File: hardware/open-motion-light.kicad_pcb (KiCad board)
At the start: 2 copper layers, 77 x 73 mm, 93 parts, among them J1 TYPE-C-31-M-12, Q1 2N7002, SW1 SW_Push, SW2 SW_Push, SW3 SSSS213800, U1 CN3058E, U2 VCNL4020-GS08, U3 MT9284BS6, U4 PIR223D-S0, U6 CH340X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

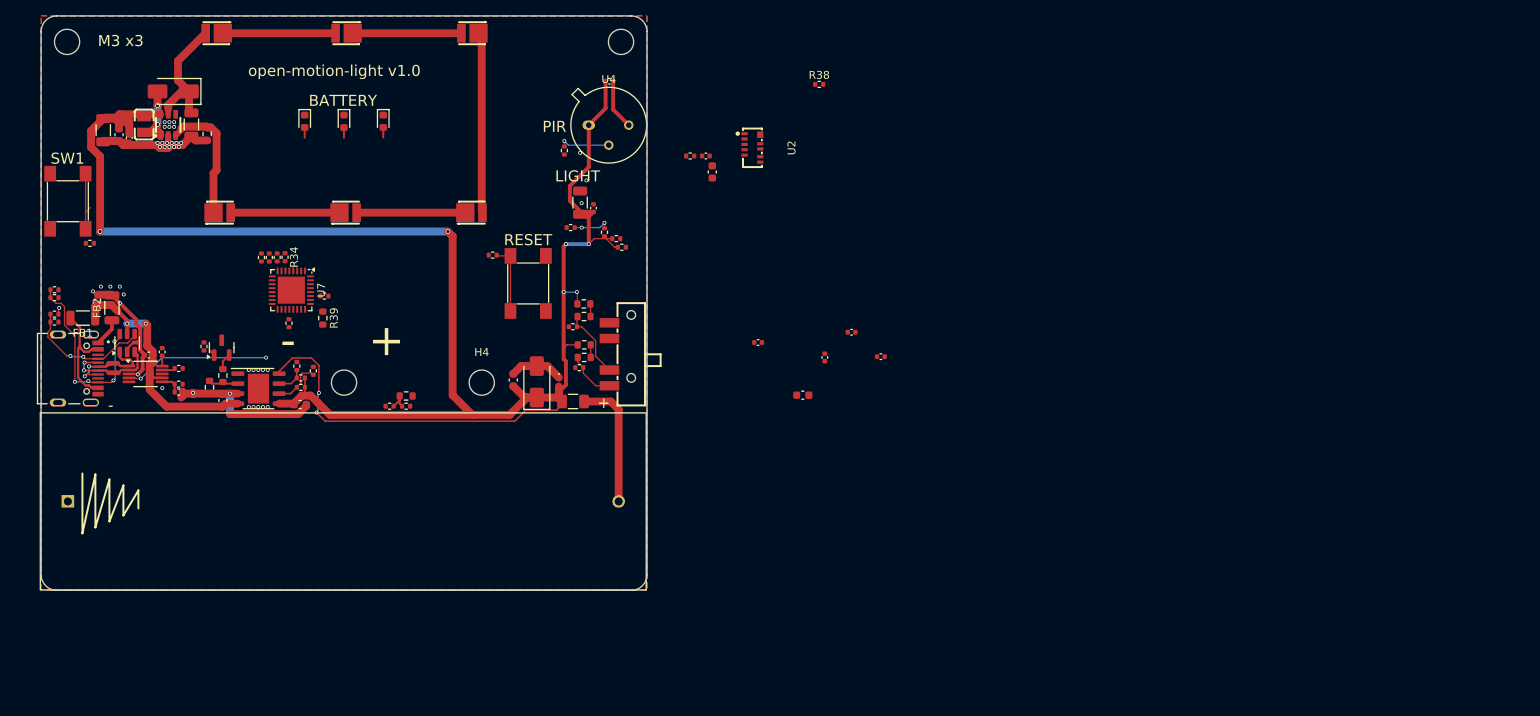
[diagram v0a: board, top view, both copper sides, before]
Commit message: Update PCB for circle layout
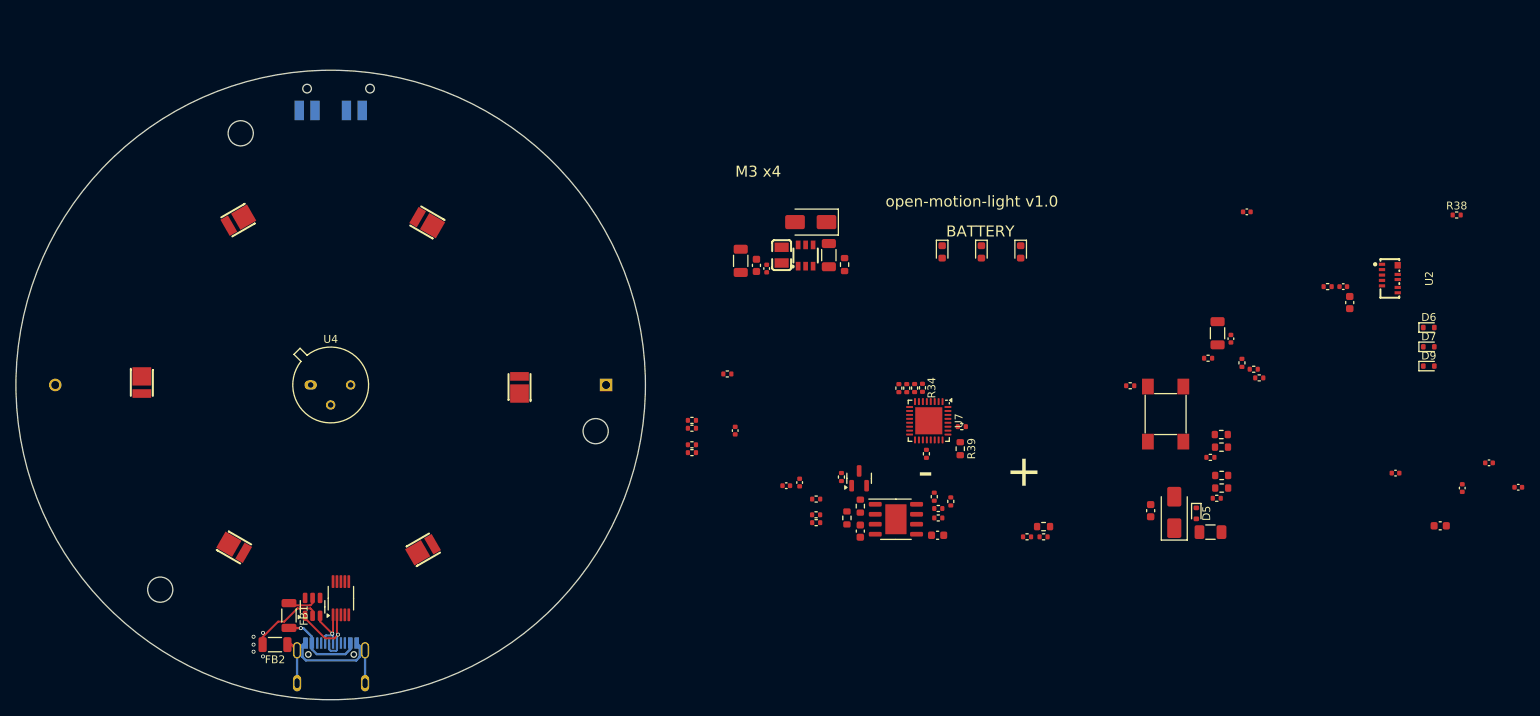
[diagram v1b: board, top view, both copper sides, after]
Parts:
- removed H4: MountingHole, MountingHole:MountingHole_3.2mm_M3_ISO7380
- removed R17: 1k, Resistor_SMD:R_0402_1005Metric
- removed SW2: SW_Push, Homebrew:SW_TACTILE_5.1MM_TS-1187A-C-D-B
- added D6: ESD5Z5.0, Diode_SMD:D_SOD-523, F.Cu at (227.4, 102.6)
- added D7: ESD5Z5.0, Diode_SMD:D_SOD-523, F.Cu at (227.4, 105.0)
- added D9: ESD5Z5.0, Diode_SMD:D_SOD-523, F.Cu at (227.4, 107.5)
- BT1, J1, SW3: moved to B.Cu
- D5: value D_TVS -> ESD5Z5.0; footprint Diode_SMD:D_0402_1005Metric -> Diode_SMD:D_SOD-523
- F1: value Polyfuse 1A -> BSMD1206-100-6V
- R2: value 1k2 -> 1k5
- R26, R30, R31: value 1k -> 10k
- moved C1 82.7 mm to (155.1, 128.5)
- moved C11 82.7 mm to (151.1, 93.4)
- moved C12 82.7 mm to (216.5, 97.4)
- moved C7 82.7 mm to (231.6, 123.0)
- moved F1 82.7 mm to (199.6, 128.6)
- moved L2 82.7 mm to (145.1, 93.4)
- moved R18 82.7 mm to (203.6, 107.1)
- moved R2 82.7 mm to (155.1, 125.3)
- moved R20 82.7 mm to (205.1, 107.9)
- moved R25 82.7 mm to (153.1, 94.6)
- moved R36 82.7 mm to (201.0, 116.2)
- moved R38 82.7 mm to (230.9, 88.3)
- moved R8 82.7 mm to (166.6, 124.7)
- moved C16 82.7 mm to (147.4, 122.3)
- moved C18 82.7 mm to (202.2, 104.0)
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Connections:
- D1 pad 1: /USB_DP -> /USB_DN
- D1 pad 3: /USB_DN -> /USB_DP
- D5 pad 1: GND -> Net-(D5-K)
- D5 pad 2: VCC -> GND
- J1 pad S1: unconnected-(J1-SHIELD-PadS1) -> Net-(FB2-Pad1)
- J1 pad S2: unconnected-(J1-SHIELD-PadS1)_2 -> Net-(FB2-Pad1)
- J1 pad S3: unconnected-(J1-SHIELD-PadS1)_1 -> Net-(FB2-Pad1)
- J1 pad S4: unconnected-(J1-SHIELD-PadS1)_0 -> Net-(FB2-Pad1)
- R26 pad 1: Net-(R26-Pad1) -> Net-(D9-K)
- R26 pad 2: /BUTTON -> /PIR
- R28 pad 2: Net-(R28-Pad2) -> Net-(D5-K)
- R31 pad 1: Net-(R28-Pad2) -> Net-(D5-K)
- SW3 pad 2: Net-(R28-Pad2) -> Net-(D5-K)
- U4 pad 2: Net-(U4-RELOUT) -> Net-(D9-K)
- U7 pad 23: /SWDIO -> unconnected-(U7-PA13-Pad23)
- U7 pad 24: /SWCLK -> unconnected-(U7-PA14-Pad24)
- U7 pad 28: /BUTTON -> unconnected-(U7-PB5-Pad28)
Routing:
- net VCC: track 254.3 -> 0.00 mm, vias 8 -> 0
- net GND: track 73.9 -> 9.59 mm, vias 40 -> 5
- net +5V: track 36.6 -> 4.24 mm, vias 2 -> 0
- net /CC2_RAW: track 24.4 -> 0.00 mm, vias 4 -> 0
- net Net-(LED3-Pad1): track 23.0 -> 0.00 mm
- net Net-(FB2-Pad1): track 3.63 -> 23.7 mm
- net Net-(U3-FB): track 19.4 -> 0.00 mm
- net /~{RTS}: track 18.6 -> 0.00 mm, vias 2 -> 0
- net /CC1_RAW: track 17.3 -> 0.00 mm, vias 2 -> 0
- net Net-(D8-K): track 16.8 -> 0.00 mm
- net Net-(BT1-Pad2): track 16.5 -> 0.00 mm
- net Net-(LED1-Pad1): track 14.3 -> 0.00 mm
- net Net-(LED5-Pad1): track 13.8 -> 0.00 mm
- net Net-(LED4-Pad1): track 13.8 -> 0.00 mm
- net Net-(LED2-Pad1): track 13.8 -> 0.00 mm
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- added copper zone on In1.Cu, net GND
- added copper zone on In2.Cu, net GND
- removed copper zone on B.Cu, net GND
- removed copper zone on F.Cu, net GND
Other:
- board size 77 x 73 mm -> 80 x 80 mm
- copper layers 2 -> 4
- board text added: "M3 x4"
- board text removed: "LIGHT"
- board text removed: "M3 x3"
- board text removed: "PIR"
- board text removed: "RESET"
- board text removed: "SW1"

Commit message: Place and route LEDs, driver, and USB power
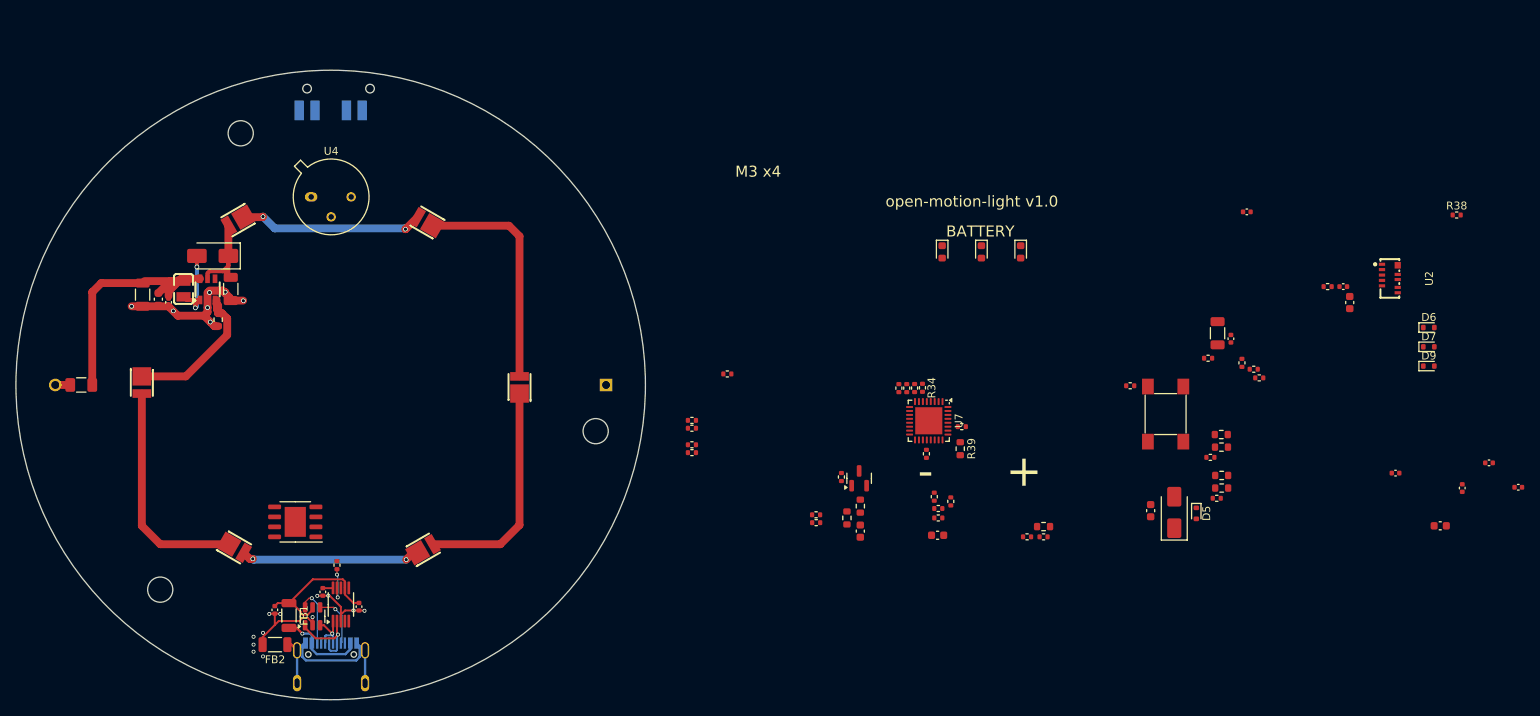
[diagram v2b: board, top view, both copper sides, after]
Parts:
- moved F1 144.7 mm to (56.1, 109.9), turned to 180 degrees
- moved R25 79.9 mm to (73.5, 101.6)
- moved U1 76.3 mm to (83.3, 127.3), turned to 180 degrees
- moved C11 76.1 mm to (75.1, 97.7)
- moved L2 76.1 mm to (69.1, 97.7)
- moved C9 76.1 mm to (67.2, 99.4)
- moved D8 76.1 mm to (72.8, 93.5)
- moved C10 76.1 mm to (65.9, 99.0)
- moved C13 76.1 mm to (63.9, 98.4)
- moved U3 76.1 mm to (72.2, 97.8)
- moved C2 62.8 mm to (80.7, 138.5), turned to -90 degrees
- moved C16 62.2 mm to (86.8, 136.2), turned to -90 degrees
- moved R22 61.5 mm to (88.6, 132.8), turned to 90 degrees
- moved C15 56.4 mm to (91.4, 138.1), turned to -90 degrees
- moved U4 23.9 mm to (85.3, 86.0)
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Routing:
- net GND: track 9.59 -> 59.2 mm, vias 5 -> 19
- net VCC: track 0.00 -> 38.5 mm
- net Net-(LED2-Pad1): track 0.00 -> 29.4 mm
- net Net-(LED5-Pad1): track 0.00 -> 28.8 mm
- net Net-(LED3-Pad1): track 0.00 -> 28.8 mm
- net Net-(LED1-Pad1): track 0.00 -> 23.4 mm, vias 0 -> 2
- net Net-(LED4-Pad1): track 0.00 -> 22.8 mm, vias 0 -> 2
- net Net-(U3-FB): track 0.00 -> 20.2 mm
- net +5V: track 4.24 -> 19.2 mm
- net Net-(D8-K): track 0.00 -> 13.0 mm
- net Net-(D8-A): track 0.00 -> 11.4 mm, vias 0 -> 2
- net /CC2_RAW: track 0.00 -> 7.71 mm, vias 0 -> 1
- net /CC1_RAW: track 0.00 -> 6.75 mm, vias 0 -> 1
- net Net-(U6-RXD): track 0.00 -> 4.89 mm, vias 0 -> 2
- net Net-(BT1-Pad2): track 0.00 -> 1.90 mm
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
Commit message: Hardware revision v1.1
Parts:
- R11, R12: value 1k -> 10k
- moved D6 169.4 mm to (58.2, 111.8)
- moved C6 164.1 mm to (74.7, 118.8), turned to 0 degrees
- moved C5 155.9 mm to (79.3, 111.5)
- moved C7 155.5 mm to (76.6, 111.1)
- moved R38 155.4 mm to (76.8, 108.5)
- moved C4 150.6 mm to (79.3, 109.7)
- moved D7 145.1 mm to (84.8, 78.0), turned to -90 degrees
- moved D9 142.2 mm to (85.9, 93.0), turned to 180 degrees
- moved U2 139.6 mm to (87.8, 133.5), turned to 180 degrees
- moved C20 138.2 mm to (83.4, 133.4)
- moved C12 136.6 mm to (84.6, 133.0), turned to 90 degrees
- moved D13 135.9 mm to (59.6, 114.4), turned to 0 degrees
- moved C8 134.9 mm to (58.3, 107.9), turned to 0 degrees
- moved R37 134.1 mm to (84.7, 131.0), turned to 90 degrees
- moved C17 132.5 mm to (91.9, 139.6)
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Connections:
- C6 pad 1: VCC -> GND
- C6 pad 2: GND -> VCC
- R37 pad 1: VCC -> Net-(U2-VDD)
- R37 pad 2: Net-(U2-VDD) -> VCC
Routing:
- net VCC: track 38.5 -> 275.4 mm, vias 0 -> 19
- net GND: track 59.2 -> 145.2 mm, vias 19 -> 187
- net Net-(D4-A): track 0.00 -> 72.0 mm, vias 0 -> 2
- net Net-(D3-A): track 0.00 -> 68.8 mm, vias 0 -> 2
- net /POWER_ON: track 0.00 -> 68.2 mm, vias 0 -> 4
- net Net-(D2-A): track 0.00 -> 65.2 mm, vias 0 -> 2
- net /POWER_AUTO: track 0.00 -> 58.2 mm, vias 0 -> 2
- net Net-(U7-NRST): track 0.00 -> 55.0 mm, vias 0 -> 6
- net Net-(U6-TXD): track 0.00 -> 46.2 mm, vias 0 -> 4
- net /USART_TX: track 0.00 -> 42.8 mm, vias 0 -> 4
- net /PIR: track 0.00 -> 40.4 mm, vias 0 -> 2
- net /BOOT0: track 0.00 -> 39.5 mm, vias 0 -> 2
- net /SDA: track 0.00 -> 38.9 mm, vias 0 -> 4
- net +5V: track 19.2 -> 57.7 mm, vias 0 -> 6
- net /SCL: track 0.00 -> 37.6 mm, vias 0 -> 4
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- added copper zone on B.Cu, net GND
- added copper zone on F.Cu, net GND
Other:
- board text added: "5V 1A MAX"
- board text added: "AUTO"
- board text added: "LiFePO4 ONLY!"
- board text added: "M3 x3"
- board text added: "OFF"
- board text added: "ON"
- board text added: "RESET"
- board text added: "open-motion-light v1.1"
- board text removed: "BATTERY"
- board text removed: "M3 x4"
- board text removed: "open-motion-light v1.0"
- board text removed: "{ "ViaStitching": "0.2", "stitch_zone_0": { "HSpacing": "5", "VSpacing": "5", "Clearance": "0.5", "Randomize": false } }"

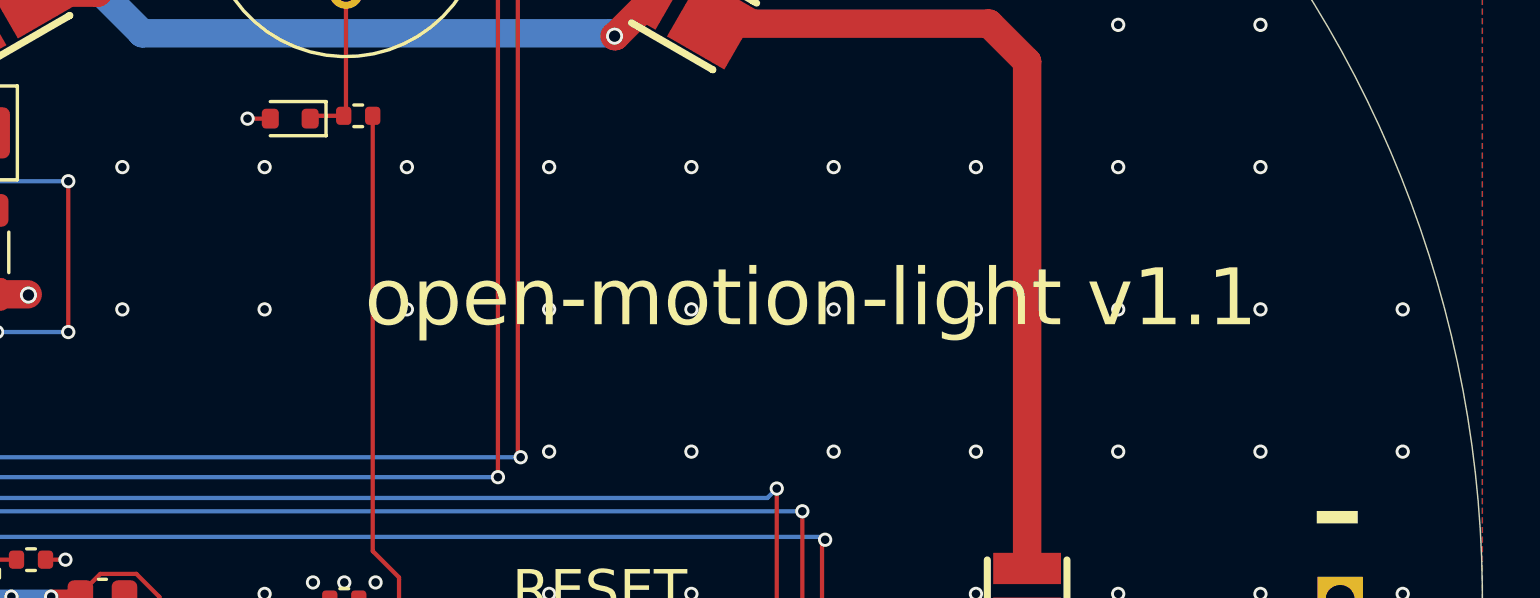
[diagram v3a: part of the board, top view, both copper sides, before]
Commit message: Start updating schematic for v1.2
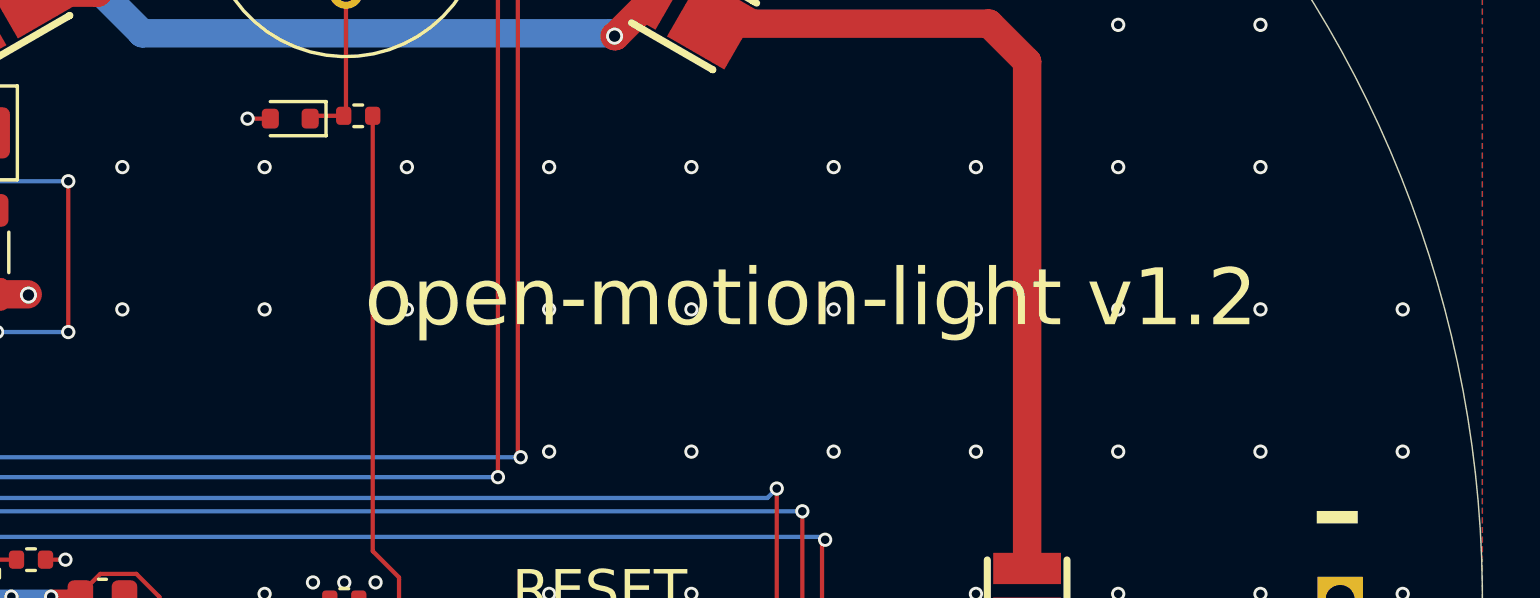
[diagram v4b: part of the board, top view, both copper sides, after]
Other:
- board text added: "open-motion-light v1.2"
- board text removed: "open-motion-light v1.1"

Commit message: Tentative hardware v1.2
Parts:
- removed D9: ESD5Z5.0, Diode_SMD:D_SOD-523
- added C21: 10uF, Capacitor_SMD:C_0603_1608Metric, F.Cu at (108.2, 92.8)
- added C22: 47uF, Capacitor_SMD:C_1206_3216Metric, F.Cu at (106.2, 92.7)
- added R17: 100k, Resistor_SMD:R_0402_1005Metric, F.Cu at (119.2, 103.8)
- added R40: 10k, Resistor_SMD:R_0603_1608Metric_Pad0.98x0.95mm_HandSolder, F.Cu at (105.3, 95.9)
- added R41: 2M, Resistor_SMD:R_0603_1608Metric, F.Cu at (109.5, 98.3)
- added R42: 330k, Resistor_SMD:R_0603_1608Metric, F.Cu at (108.6, 95.9)
- R26: value 10k -> 1k
- R27, R8, R9: value 1k -> 1k
- R39: value 2M -> 22k; footprint Resistor_SMD:R_0603_1608Metric -> Resistor_SMD:R_0402_1005Metric
- SW1: moved to B.Cu
- U4: value PIR223D-S0 -> XYC-PIR224S-S1; footprint Homebrew:PIR223D-S0 -> easyeda2kicad:TO-5-4_BD9.2-P2.54_XYC-PIR224D-D0
- moved SW1 41.9 mm to (62.1, 91.8)
- moved U4 32.2 mm to (116.8, 92.8), turned to 90 degrees
- moved R26 32.2 mm to (119.2, 101.8), turned to 90 degrees
- moved C14 29.5 mm to (109.5, 92.8)
- moved R13 28.9 mm to (64.8, 104.2), turned to 0 degrees
- moved R39 10.3 mm to (85.1, 108.6), turned to 0 degrees
- moved R38 9.12 mm to (70.1, 114.7), turned to -90 degrees
- moved H2 7.78 mm to (115.2, 133.1)
- moved R34 5.96 mm to (72.4, 114.2), turned to 0 degrees
- moved D4 3.15 mm to (101.6, 145.8)
- moved D2 2.93 mm to (106.1, 143.7)
- moved D3 2.91 mm to (103.9, 144.8)
- moved H3 2.14 mm to (64.6, 137.4)
- moved H1 2.03 mm to (75.7, 76.0)
- moved J1 0.48 mm to (87.8, 145.8)
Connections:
- C14 pad 1: VCC -> Net-(U4-VDD)
- R26 pad 1: Net-(D9-K) -> /PIR
- R26 pad 2: /PIR -> Net-(U4-REL)
- R39 pad 1: Net-(U7-PA15) -> Net-(U7-PA0)
- U4 pad 1: VCC -> GND
- U4 pad 2: Net-(D9-K) -> Net-(U4-SENS)
- U4 pad 3: GND -> Net-(U4-VDD)
- U7 pad 11: /POWER_ON -> /WHITE_LED
- U7 pad 14: unconnected-(U7-PB0-Pad14) -> /POWER_ON
- U7 pad 25: Net-(U7-PA15) -> unconnected-(U7-PA15-Pad25)
- U7 pad 6: /WHITE_LED -> Net-(U7-PA0)
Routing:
- net VCC: track 275.4 -> 309.0 mm, vias 19 -> 20
- net Net-(U7-NRST): track 55.0 -> 77.4 mm, vias 6 -> 7
- net /POWER_ON: track 68.2 -> 50.2 mm, vias 4 -> 2
- net /PIR: track 40.4 -> 58.2 mm
- net Net-(U4-VDD): track 0.00 -> 17.4 mm
- net Net-(U7-PA0): track 0.00 -> 13.6 mm, vias 0 -> 2
- net Net-(U4-REL): track 0.00 -> 8.38 mm
- net Net-(U4-SENS): track 0.00 -> 7.33 mm, vias 0 -> 1
- net Net-(LED5-Pad1): track 30.5 -> 24.0 mm
- net Net-(LED3-Pad1): track 30.1 -> 24.1 mm
- net Net-(LED2-Pad1): track 29.4 -> 23.7 mm
- net Net-(D9-K): track 5.61 -> 0.00 mm
- net GND: track 145.2 -> 141.2 mm, vias 187 -> 75
- net Net-(D2-A): track 65.2 -> 68.4 mm
- net Net-(U3-EN): track 22.4 -> 25.4 mm, vias 4 -> 0
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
